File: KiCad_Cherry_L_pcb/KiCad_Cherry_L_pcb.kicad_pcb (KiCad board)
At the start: 2 copper layers, 135.7 x 97.6 mm, 0 parts

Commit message: refactor: 作り直し
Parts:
- added C1: C, Capacitor_SMD:C_0805_2012Metric, B.Cu at (205.4, 106.2)
- added C2: C, Capacitor_SMD:C_0805_2012Metric, B.Cu at (95.8, 69.1)
- added D1: 1N4148W, Diode_SMD:D_SOD-323, B.Cu at (88.1, 54.8)
- added D10: 1N4148W, Diode_SMD:D_SOD-323, B.Cu at (154.8, 73.8)
- added D11: 1N4148W, Diode_SMD:D_SOD-323, B.Cu at (173.8, 73.8)
- added D12: 1N4148W, Diode_SMD:D_SOD-323, B.Cu at (192.9, 73.8)
- added D13: 1N4148W, Diode_SMD:D_SOD-323, B.Cu at (95.2, 92.9)
- added D14: 1N4148W, Diode_SMD:D_SOD-323, B.Cu at (121.4, 92.9)
- added D15: 1N4148W, Diode_SMD:D_SOD-323, B.Cu at (140.5, 92.9)
- added D16: 1N4148W, Diode_SMD:D_SOD-323, B.Cu at (159.5, 92.9)
- added D17: 1N4148W, Diode_SMD:D_SOD-323, B.Cu at (178.6, 92.9)
- added D18: 1N4148W, Diode_SMD:D_SOD-323, B.Cu at (197.6, 92.9)
- added D19: 1N4148W, Diode_SMD:D_SOD-323, B.Cu at (100.0, 111.9)
- added D2: 1N4148W, Diode_SMD:D_SOD-323, B.Cu at (107.2, 54.8)
- added D20: 1N4148W, Diode_SMD:D_SOD-323, B.Cu at (131.0, 111.9)
- added D21: 1N4148W, Diode_SMD:D_SOD-323, B.Cu at (150.0, 111.9)
- added D22: 1N4148W, Diode_SMD:D_SOD-323, B.Cu at (169.1, 111.9)
- added D23: 1N4148W, Diode_SMD:D_SOD-323, B.Cu at (188.1, 111.9)
- added D24: 1N4148W, Diode_SMD:D_SOD-323, B.Cu at (202.4, 54.8)
- added D25: 1N4148W, Diode_SMD:D_SOD-323, B.Cu at (90.5, 131.0)
- added D26: 1N4148W, Diode_SMD:D_SOD-323, B.Cu at (114.3, 131.0)
- added D27: 1N4148W, Diode_SMD:D_SOD-323, B.Cu at (138.1, 131.0)
- added D28: 1N4148W, Diode_SMD:D_SOD-323, B.Cu at (161.9, 131.0)
- added D29: 1N4148W, Diode_SMD:D_SOD-323, B.Cu at (192.9, 131.0)
- added D3: 1N4148W, Diode_SMD:D_SOD-323, B.Cu at (126.2, 54.8)
- added D30: 1N4148W, Diode_SMD:D_SOD-323, B.Cu at (203.0, 106.1)
- added D4: 1N4148W, Diode_SMD:D_SOD-323, B.Cu at (145.3, 54.8)
- added D5: 1N4148W, Diode_SMD:D_SOD-323, B.Cu at (164.3, 54.8)
- added D6: 1N4148W, Diode_SMD:D_SOD-323, B.Cu at (183.4, 54.8)
- added D7: 1N4148W, Diode_SMD:D_SOD-323, B.Cu at (92.9, 73.8)
- added D8: 1N4148W, Diode_SMD:D_SOD-323, B.Cu at (116.7, 73.8)
- added D9: 1N4148W, Diode_SMD:D_SOD-323, B.Cu at (135.7, 73.8)
- added H10: MountingHole_2.2mm_M2, MountingHole:MountingHole_2.2mm_M2, F.Cu at (207.2, 47.6)
- added H12: MountingHole_2.2mm_M2, MountingHole:MountingHole_2.2mm_M2, F.Cu at (169.1, 142.9)
- added H13: MountingHole_2.2mm_M2, MountingHole:MountingHole_2.2mm_M2, F.Cu at (207.2, 142.9)
- added H14: MountingHole_2.2mm_M2, MountingHole:MountingHole_2.2mm_M2, F.Cu at (216.7, 123.8)
- added H2: MountingHole_2.2mm_M2, MountingHole:MountingHole_2.2mm_M2, F.Cu at (92.9, 47.6)
- added H2: MountingHole_2.2mm_M2, MountingHole:MountingHole_2.2mm_M2, F.Cu at (92.9, 142.9)
- added H2: MountingHole_2.2mm_M2, MountingHole:MountingHole_2.2mm_M2, F.Cu at (131.0, 142.9)
- added H2: MountingHole_2.2mm_M2, MountingHole:MountingHole_2.2mm_M2, F.Cu at (216.7, 95.2)
- added H2: MountingHole_2.2mm_M2, MountingHole:MountingHole_2.2mm_M2, F.Cu at (83.3, 95.2)
- added H3: MountingHole_2.2mm_M2, MountingHole:MountingHole_2.2mm_M2, F.Cu at (131.0, 47.6)
- added H4: MountingHole_2.2mm_M2, MountingHole:MountingHole_2.2mm_M2, F.Cu at (169.1, 47.6)
- added H7: MountingHole_2.2mm_M2, MountingHole:MountingHole_2.2mm_M2, F.Cu at (83.3, 66.7)
- added H8: MountingHole_2.2mm_M2, MountingHole:MountingHole_2.2mm_M2, F.Cu at (216.7, 66.7)
- added H9: MountingHole_2.2mm_M2, MountingHole:MountingHole_2.2mm_M2, F.Cu at (83.3, 123.8)
- added J1: AudioJack3_SwitchTR, Connector_Audio:Jack_3.5mm_CUI_SJ1-3515N_Horizontal, B.Cu at (213.8, 114.3)
- added SW1: Esc, KBD_BrownSugar:CherryMX_Hotswap_via_1U, F.Cu at (92.9, 57.1)
- added SW10: E, KBD_BrownSugar:CherryMX_Hotswap_via_1U, F.Cu at (159.5, 76.2)
- added SW11: R, KBD_BrownSugar:CherryMX_Hotswap_via_1U, F.Cu at (178.5, 76.2)
- added SW12: T, KBD_BrownSugar:CherryMX_Hotswap_via_1U, F.Cu at (197.6, 76.2)
- added SW13: Ctrl, KBD_BrownSugar:CherryMX_Hotswap_via_1.75U, F.Cu at (100.0, 95.2)
- added SW14: A, KBD_BrownSugar:CherryMX_Hotswap_via_1U, F.Cu at (126.2, 95.2)
- added SW15: S, KBD_BrownSugar:CherryMX_Hotswap_via_1U, F.Cu at (145.3, 95.2)
- added SW16: D, KBD_BrownSugar:CherryMX_Hotswap_via_1U, F.Cu at (164.3, 95.2)
- added SW17: F, KBD_BrownSugar:CherryMX_Hotswap_via_1U, F.Cu at (183.4, 95.2)
- added SW18: G, KBD_BrownSugar:CherryMX_Hotswap_via_1U, F.Cu at (202.4, 95.2)
- added SW19: Shift, KBD_BrownSugar:CherryMX_Hotswap_via_2.25U, F.Cu at (104.8, 114.3)
- added SW2: 1, KBD_BrownSugar:CherryMX_Hotswap_via_1U, F.Cu at (111.9, 57.1)
- added SW20: Z, KBD_BrownSugar:CherryMX_Hotswap_via_1U, F.Cu at (135.7, 114.3)
- added SW21: X, KBD_BrownSugar:CherryMX_Hotswap_via_1U, F.Cu at (154.8, 114.3)
- added SW22: C, KBD_BrownSugar:CherryMX_Hotswap_via_1U, F.Cu at (173.8, 114.3)
- added SW23: V, KBD_BrownSugar:CherryMX_Hotswap_via_1U, F.Cu at (192.9, 114.3)
- added SW24: 6, KBD_BrownSugar:CherryMX_Hotswap_via_1U, F.Cu at (207.2, 57.1)
- added SW25: Fn, KBD_BrownSugar:CherryMX_Hotswap_via_1.25U, F.Cu at (95.3, 133.3)
- added SW26: Alt, KBD_BrownSugar:CherryMX_Hotswap_via_1.25U, F.Cu at (119.1, 133.3)
- added SW27: Win, KBD_BrownSugar:CherryMX_Hotswap_via_1.25U, F.Cu at (142.8, 133.3)
- added SW28: NoConv, KBD_BrownSugar:CherryMX_Hotswap_via_1.25U, F.Cu at (166.7, 133.3)
- added SW29: Space, KBD_BrownSugar:CherryMX_Hotswap_via_2U, F.Cu at (197.6, 133.3)
- added SW3: 2, KBD_BrownSugar:CherryMX_Hotswap_via_1U, F.Cu at (131.0, 57.1)
- added SW4: 3, KBD_BrownSugar:CherryMX_Hotswap_via_1U, F.Cu at (150.0, 57.1)
- added SW5: 4, KBD_BrownSugar:CherryMX_Hotswap_via_1U, F.Cu at (169.1, 57.1)
- added SW6: 5, KBD_BrownSugar:CherryMX_Hotswap_via_1U, F.Cu at (188.1, 57.1)
- added SW7: Tab, KBD_BrownSugar:CherryMX_Hotswap_via_1.5U, F.Cu at (97.6, 76.2)
- added SW8: Q, KBD_BrownSugar:CherryMX_Hotswap_via_1U, F.Cu at (121.4, 76.2)
- added SW9: W, KBD_BrownSugar:CherryMX_Hotswap_via_1U, F.Cu at (140.5, 76.2)
- added U1: Sparkfun_Pro_Micro, Arduino:Sparkfun_Pro_Micro, B.Cu at (117.8, 67.0)
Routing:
- added copper zone on B.Cu, net GND
- added copper zone on F.Cu, net GND
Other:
- board size 135.7 x 97.6 mm -> 138.1 x 100 mm
- board text added: "J2J - Left"
- board text added: "JLCJLCJLCJLC"

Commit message: feat: Rightの配置が完了
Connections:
- U1 pad 12: +5V -> unconnected-(U1-~D9/A9-Pad12)
- U1 pad 13: unconnected-(U1-~D10/A10-Pad13) -> +5V
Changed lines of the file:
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@@
 	(net 39 "unconnected-(J1-PadRN)")
 	(net 40 "SCL")
-	(net 41 "unconnected-(U1-~D10{slash}A10-Pad13)")
+	(net 41 "unconnected-(U1-~D9{slash}A9-Pad12)")
 	(net 42 "Col0")
 	(net 43 "Col1")
@@
 			(layers "*.Cu" "*.Mask")
 			(remove_unused_layers no)
-			(net 1 "+5V")
+			(net 41 "unconnected-(U1-~D9{slash}A9-Pad12)")
 			(pinfunction "~D9/A9")
-			(pintype "bidirectional")
+			(pintype "bidirectional+no_connect")
 		)
 		(pad "13" thru_hole oval
@@
 			(layers "*.Cu" "*.Mask")
 			(remove_unused_layers no)
-			(net 41 "unconnected-(U1-~D10{slash}A10-Pad13)")
+			(net 1 "+5V")
 			(pinfunction "~D10/A10")
-			(pintype "bidirectional+no_connect")
+			(pintype "bidirectional")
 		)
 		(pad "14" thru_hole oval
@@
 			(net 49 "unconnected-(U1-RST-Pad22)")
 			(pinfunction "RST")
-			(pintype "input")
+			(pintype "input+no_connect")
 		)
 		(pad "23" thru_hole oval

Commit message: feat: Resetピンを追加
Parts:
- added J2: Reset, Connector_PinHeader_1.00mm:PinHeader_1x01_P1.00mm_Vertical, F.Cu at (82.2, 59.5)
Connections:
- U1 pad 22: unconnected-(U1-RST-Pad22) -> Net-(J2-Pin_1)
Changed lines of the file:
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@@
 	(net 47 "Col5")
 	(net 48 "unconnected-(U1-RAW-Pad24)")
-	(net 49 "unconnected-(U1-RST-Pad22)")
+	(net 49 "Net-(J2-Pin_1)")
 	(net 50 "unconnected-(U1-D1{slash}TX-Pad1)")
 	(net 51 "unconnected-(U1-D0{slash}RX-Pad2)")
@@
 		)
 	)
+	(footprint "Connector_PinHeader_1.00mm:PinHeader_1x01_P1.00mm_Vertical"
+		(layer "F.Cu")
+		(at 82.153194 59.5313 90)
+		(descr "Through hole straight pin header, 1x01, 1.00mm pitch, single row")
+		(tags "Through hole pin header THT 1x01 1.00mm single row")
+		(property "Reference" "J2"
+			(at 0 -1.61 90)
+			(layer "F.SilkS")
+			(hide yes)
+			(effects
+				(font
+					(size 1 1)
+					(thickness 0.15)
+				)
+			)
+		)
+		(property "Value" "Reset"
+			(at 0 1.61 90)
+			(layer "F.Fab")
+			(hide yes)
+			(effects
+				(font
+					(size 1 1)
+					(thickness 0.15)
+				)
+			)
+		)
+		(property "Datasheet" "~"
+			(at 0 0 90)
+			(layer "F.Fab")
+			(hide yes)
+			(effects
+				(font
+					(size 1.27 1.27)
+					(thickness 0.15)
+				)
+			)
+		)
+		(property "Description" "Generic connector, single row, 01x01, script generated"
+			(at 0 0 90)
+			(layer "F.Fab")
+			(hide yes)
+			(effects
+				(font
+					(size 1.27 1.27)
+					(thickness 0.15)
+				)
+			)
+		)
+		(property ki_fp_filters "Connector*:*_1x??_*")
+		(sheetname "/")
+		(sheetfile "KiCad_Cherry_L_pcb.kicad_sch")
+		(attr through_hole)
+		(fp_line
+			(start -0.745 -0.735)
+			(end 0 -0.735)
+			(stroke
+				(width 0.12)
+				(type solid)
+			)
+			(layer "F.SilkS")
+		)
+		(fp_line
+			(start -0.745 0)
+			(end -0.745 -0.735)
+			(stroke
+				(width 0.12)
+				(type solid)
+			)
+			(layer "F.SilkS")
+		)
+		(fp_line
+			(start 0.745 0.735)
+			(end 0.745 0.61)
+			(stroke
+				(width 0.12)
+				(type solid)
+			)
+			(layer "F.SilkS")
+		)
+		(fp_line
+			(start 0.685565 0.735)
+			(end 0.745 0.735)
+			(stroke
+				(width 0.12)
+				(type solid)
+			)
+			(layer "F.SilkS")
+		)
+		(fp_line
+			(start -0.745 0.735)
+			(end -0.745 0.61)
+			(stroke
+				(width 0.12)
+				(type solid)
+			)
+			(layer "F.SilkS")
+		)
+		(fp_line
+			(start -0.745 0.735)
+			(end 0.745 0.735)
+			(stroke
+				(width 0.12)
+				(type solid)
+			)
+			(layer "F.SilkS")
+		)
+		(fp_line
+			(start -0.745 0.735)
+			(end -0.685565 0.735)
+			(stroke
+				(width 0.12)
+				(type solid)
+			)
+			(layer "F.SilkS")
+		)
+		(fp_rect
+			(start -1.14 -1)
+			(end 1.14 1)
+			(stroke
+				(width 0.05)
+				(type solid)
+			)
+			(fill no)
+			(layer "F.CrtYd")
+		)
+		(fp_line
+			(start 0.635 -0.5)
+			(end 0.635 0.5)
+			(stroke
+				(width 0.1)
+				(type solid)
+			)
+			(layer "F.Fab")
+		)
+		(fp_line
+			(start -0.3175 -0.5)
+			(end 0.635 -0.5)
+			(stroke
+				(width 0.1)
+				(type solid)
+			)
+			(layer "F.Fab")
+		)
+		(fp_line
+			(start -0.635 -0.1825)
+			(end -0.3175 -0.5)
+			(stroke
+				(width 0.1)
+				(type solid)
+			)
+			(layer "F.Fab")
+		)
+		(fp_line
+			(start 0.635 0.5)
+			(end -0.635 0.5)
+			(stroke
+				(width 0.1)
+				(type solid)
+			)
+			(layer "F.Fab")
+		)
+		(fp_line
+			(start -0.635 0.5)
+			(end -0.635 -0.1825)
+			(stroke
+				(width 0.1)
+				(type solid)
+			)
+			(layer "F.Fab")
+		)
+		(fp_text user "${REFERENCE}"
+			(at 0 0 0)
+			(layer "F.Fab")
+			(effects
+				(font
+					(size 0.76 0.76)
+					(thickness 0.114)
+				)
+			)
+		)
+		(pad "1" thru_hole rect
+			(at 0 0 90)
+			(size 0.85 0.85)
+			(drill 0.5)
+			(layers "*.Cu" "*.Mask")
+			(remove_unused_layers no)
+			(net 49 "Net-(J2-Pin_1)")
+			(pinfunction "Pin_1")
+			(pintype "passive")
+		)
+		(embedded_fonts no)
+		(model "${KICAD9_3DMODEL_DIR}/Connector_PinHeader_1.00mm.3dshapes/PinHeader_1x01_P1.00mm_Vertical.step"
+			(offset
+				(xyz 0 0 0)
+			)
+			(scale
+				(xyz 1 1 1)
+			)
+			(rotate
+				(xyz 0 0 0)
+			)
+		)
+	)
 	(footprint "MountingHole:MountingHole_2.2mm_M2"
 		(layer "F.Cu")
@@
 			(layers "*.Cu" "*.Mask")
 			(remove_unused_layers no)
-			(net 49 "unconnected-(U1-RST-Pad22)")
+			(net 49 "Net-(J2-Pin_1)")
 			(pinfunction "RST")
-			(pintype "input+no_connect")
+			(pintype "input")
 		)
 		(pad "23" thru_hole oval

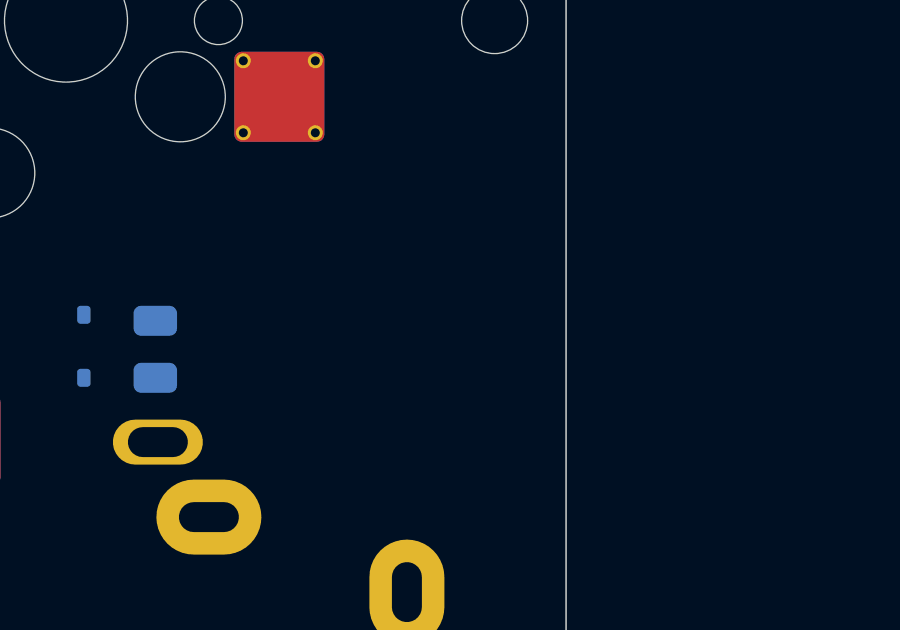
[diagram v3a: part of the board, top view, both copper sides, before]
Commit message: feat: Rightのガワを用意
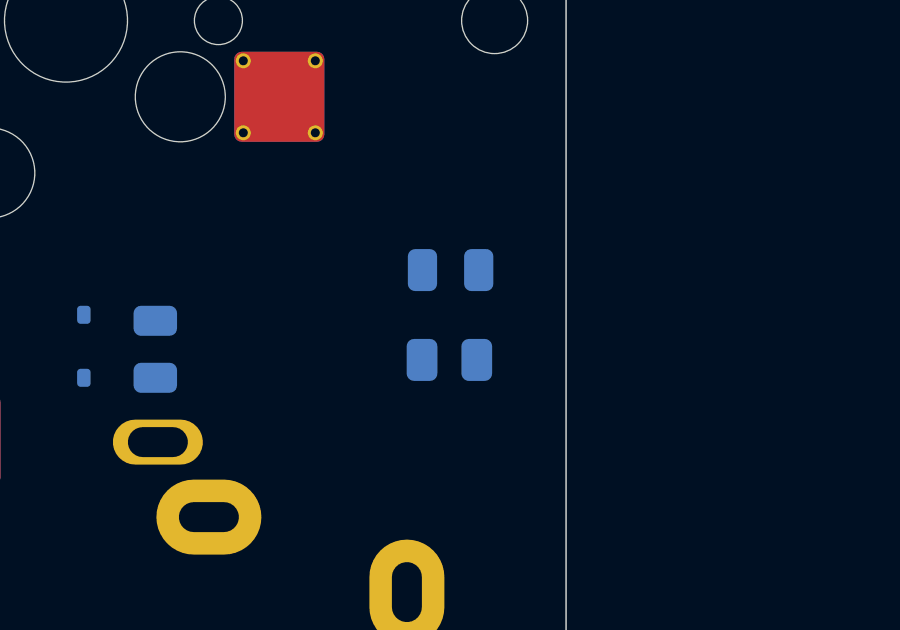
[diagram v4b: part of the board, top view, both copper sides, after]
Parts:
- added D31: LED, LED_SMD:LED_0805_2012Metric, B.Cu at (215.2, 103.6)
- added R1: 10k, Resistor_SMD:R_0805_2012Metric, B.Cu at (215.2, 106.6)
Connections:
- U1 pad 2: unconnected-(U1-D0/RX-Pad2) -> Net-(D31-A)

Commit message: feat: ガワがすべて完成
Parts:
- added H2: MountingHole_2.2mm_M2, MountingHole:MountingHole_2.2mm_M2, F.Cu at (83.3, 50.0)
- moved H2 10.7 mm to (216.7, 106.0)
- moved D31 8.31 mm to (206.9, 103.6)
- moved R1 5.94 mm to (209.3, 106.0)
- moved H7 2.38 mm to (83.3, 69.1)
- moved H14 1.19 mm to (216.7, 122.6)
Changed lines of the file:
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@@
 	(footprint "MountingHole:MountingHole_2.2mm_M2"
 		(layer "F.Cu")
+		(at 83.34375 50.00625)
+		(descr "Mounting Hole 2.2mm, M2, no annular, generated by kicad-footprint-generator mountinghole.py")
+		(tags "mountinghole M2")
+		(property "Reference" "H2"
+			(at 0 -3.15 0)
+			(layer "F.SilkS")
+			(hide yes)
+			(effects
+				(font
+					(size 1 1)
+					(thickness 0.15)
+				)
+			)
+		)
+		(property "Value" "MountingHole_2.2mm_M2"
+			(at 0 3.15 0)
+			(layer "F.Fab")
+			(hide yes)
+			(effects
+				(font
+					(size 1 1)
+					(thickness 0.15)
+				)
+			)
+		)
+		(property "Datasheet" ""
+			(at 0 0 0)
+			(layer "F.Fab")
+			(hide yes)
+			(effects
+				(font
+					(size 1.27 1.27)
+					(thickness 0.15)
+				)
+			)
+		)
+		(property "Description" ""
+			(at 0 0 0)
+			(layer "F.Fab")
+			(hide yes)
+			(effects
+				(font
+					(size 1.27 1.27)
+					(thickness 0.15)
+				)
+			)
+		)
+		(attr exclude_from_pos_files exclude_from_bom)
+		(fp_circle
+			(center 0 0)
+			(end 2.2 0)
+			(stroke
+				(width 0.15)
+				(type solid)
+			)
+			(fill no)
+			(layer "Cmts.User")
+		)
+		(fp_circle
+			(center 0 0)
+			(end 2.45 0)
+			(stroke
+				(width 0.05)
+				(type solid)
+			)
+			(fill no)
+			(layer "F.CrtYd")
+		)
+		(pad "" np_thru_hole circle
+			(at 0 0)
+			(size 2.2 2.2)
+			(drill 2.2)
+			(layers "*.Cu" "*.Mask")
+		)
+		(embedded_fonts no)
+	)
+	(footprint "MountingHole:MountingHole_2.2mm_M2"
+		(layer "F.Cu")
 		(at 92.86875 47.625)
 		(descr "Mounting Hole 2.2mm, M2, no annular, generated by kicad-footprint-generator mountinghole.py")
@@
 	(footprint "MountingHole:MountingHole_2.2mm_M2"
 		(layer "F.Cu")
-		(at 83.34375 66.675)
+		(at 83.34375 69.05625)
 		(descr "Mounting Hole 2.2mm, M2, no annular, generated by kicad-footprint-generator mountinghole.py")
 		(tags "mountinghole M2")
@@
 	(footprint "MountingHole:MountingHole_2.2mm_M2"
 		(layer "F.Cu")
-		(at 216.69375 95.25)
+		(at 216.69375 105.965625)
 		(descr "Mounting Hole 2.2mm, M2, no annular, generated by kicad-footprint-generator mountinghole.py")
 		(tags "mountinghole M2")
@@
 	(footprint "MountingHole:MountingHole_2.2mm_M2"
 		(layer "F.Cu")
-		(at 216.69375 123.825)
+		(at 216.69375 122.634375)
 		(descr "Mounting Hole 2.2mm, M2, no annular, generated by kicad-footprint-generator mountinghole.py")
 		(tags "mountinghole M2")
@@
 	(footprint "Arduino:Sparkfun_Pro_Micro"
 		(layer "B.Cu")
-		(at 117.832263 67.032231 90)
+		(at 117.7925 67.032231 90)
 		(descr "Sparkfun Pro Micro")
 		(tags "Arduino Sparkfun Pro Micro")
@@
 	(footprint "LED_SMD:LED_0805_2012Metric"
 		(layer "B.Cu")
-		(at 215.226119 103.566027 180)
+		(at 206.915625 103.566027 180)
 		(descr "LED SMD 0805 (2012 Metric), square (rectangular) end terminal, IPC-7351 nominal, (Body size source: https://docs.google.com/spreadsheets/d/1BsfQQcO9C6DZCsRaXUlFlo91Tg2WpOkGARC1WS5S8t0/edit?usp=sharing), generated with kicad-footprint-generator")
 		(tags "LED")
@@
 	(footprint "Resistor_SMD:R_0805_2012Metric"
 		(layer "B.Cu")
-		(at 215.186119 106.561027 180)
+		(at 209.271875 105.965625 180)
 		(descr "Resistor SMD 0805 (2012 Metric), square (rectangular) end terminal, IPC-7351 nominal, (Body size source: IPC-SM-782 page 72, https://www.pcb-3d.com/wordpress/wp-content/uploads/ipc-sm-782a_amendment_1_and_2.pdf), generated with kicad-footprint-generator")
 		(tags "resistor")
